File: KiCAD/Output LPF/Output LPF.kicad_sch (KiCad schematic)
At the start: 77 parts, among them J1 Conn_Coaxial_Small, J16 Screw_Terminal_01x02, J2 8P8C_Shielded, J25 Screw_Terminal_01x02, J26 Screw_Terminal_01x02, J27 Screw_Terminal_01x02, J28 Filter In, J29 Screw_Terminal_01x02, K1 Relay_RSS-SR042P, K10 Relay_RSS-SR042P, K2 Relay_RSS-SR042P, K3 Relay_RSS-SR042P, K4 Relay_RSS-SR042P, K5 Relay_RSS-SR042P, K6 Relay_RSS-SR042P, K7 Relay_RSS-SR042P, K8 Relay_RSS-SR042P, K9 Relay_RSS-SR042P, Q1 2N7000, Q10 2N7000, Q5 2N7000, Q8 2N7000, Q9 2N7000

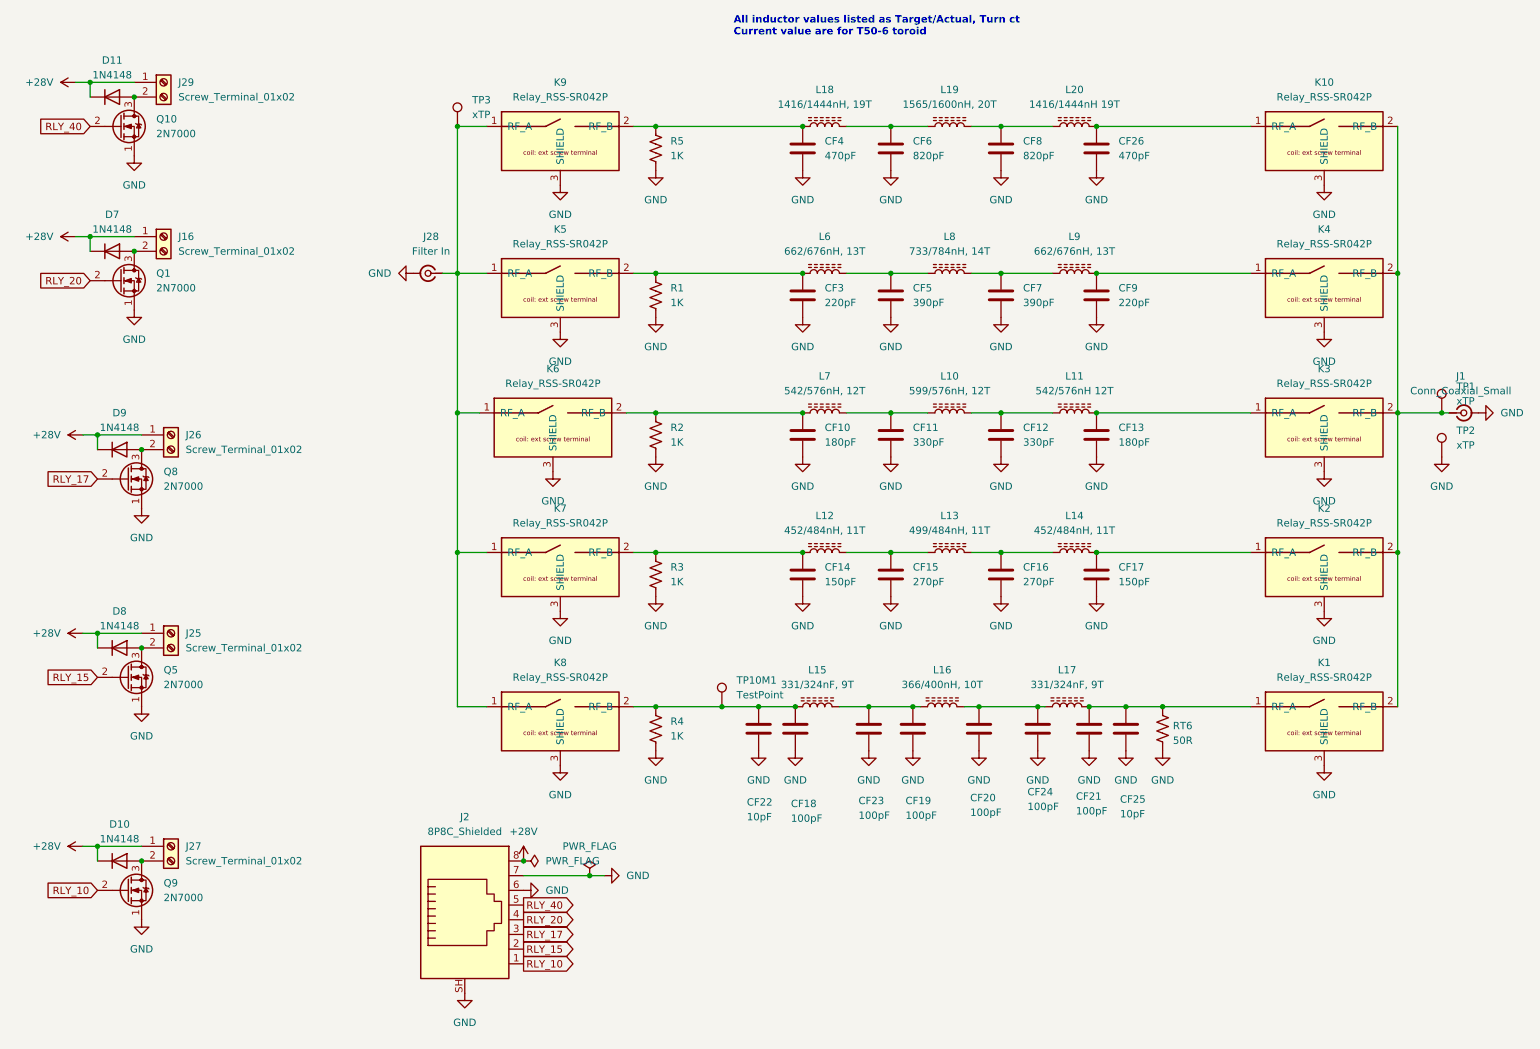
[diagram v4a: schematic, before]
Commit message: WIP revD Output LPF: 10m bank converted to G6K DPDT, library additions
Intermediate snapshot -- migration in progress.

- xmitter library: add Relay_G6K symbol (copied from stock KiCad
  Relay:G6K-2, pre-linked to xmitter:Relay_DPDT_G6K-2P-Y-T1 footprint)
  and Relay_DPDT_G6K-2P-Y-T1.kicad_mod footprint (10 x 6.5 mm body,
  -Y pitch: 3.2mm/2.2mm/2.2mm along row, 5.08mm row spacing, 0.85mm
  THT holes)
- Documentation/Components: Omron G6K-T1 datasheet
- Output LPF 10m bank: converted from K1+K8 SPST pair to single K1
  DPDT G6K. Pole 1 switches output (pin 3=COM to LPF-out, pin 4=NO
  to common J1). Pole 2 switches input (pin 6=COM to LPF-in, pin
  5=NO to common J28). K8 removed.
- Analog: WIP (details TBD when more banks converted)

Known open items before next commit:
- +12V net on LPF has no source (umbilical still carries +28V, needs
  rewire or LDO)
- 40m/20m/17m/15m banks still on old RSS-SR042P SPST topology
- Consider moving R3 to K1 pin 7 (removes 0.4 dB active-path loss,
  keeps swamp function via NC path when bank unselected)

Co-Authored-By: Claude Opus 4.7 <noreply@anthropic.com>
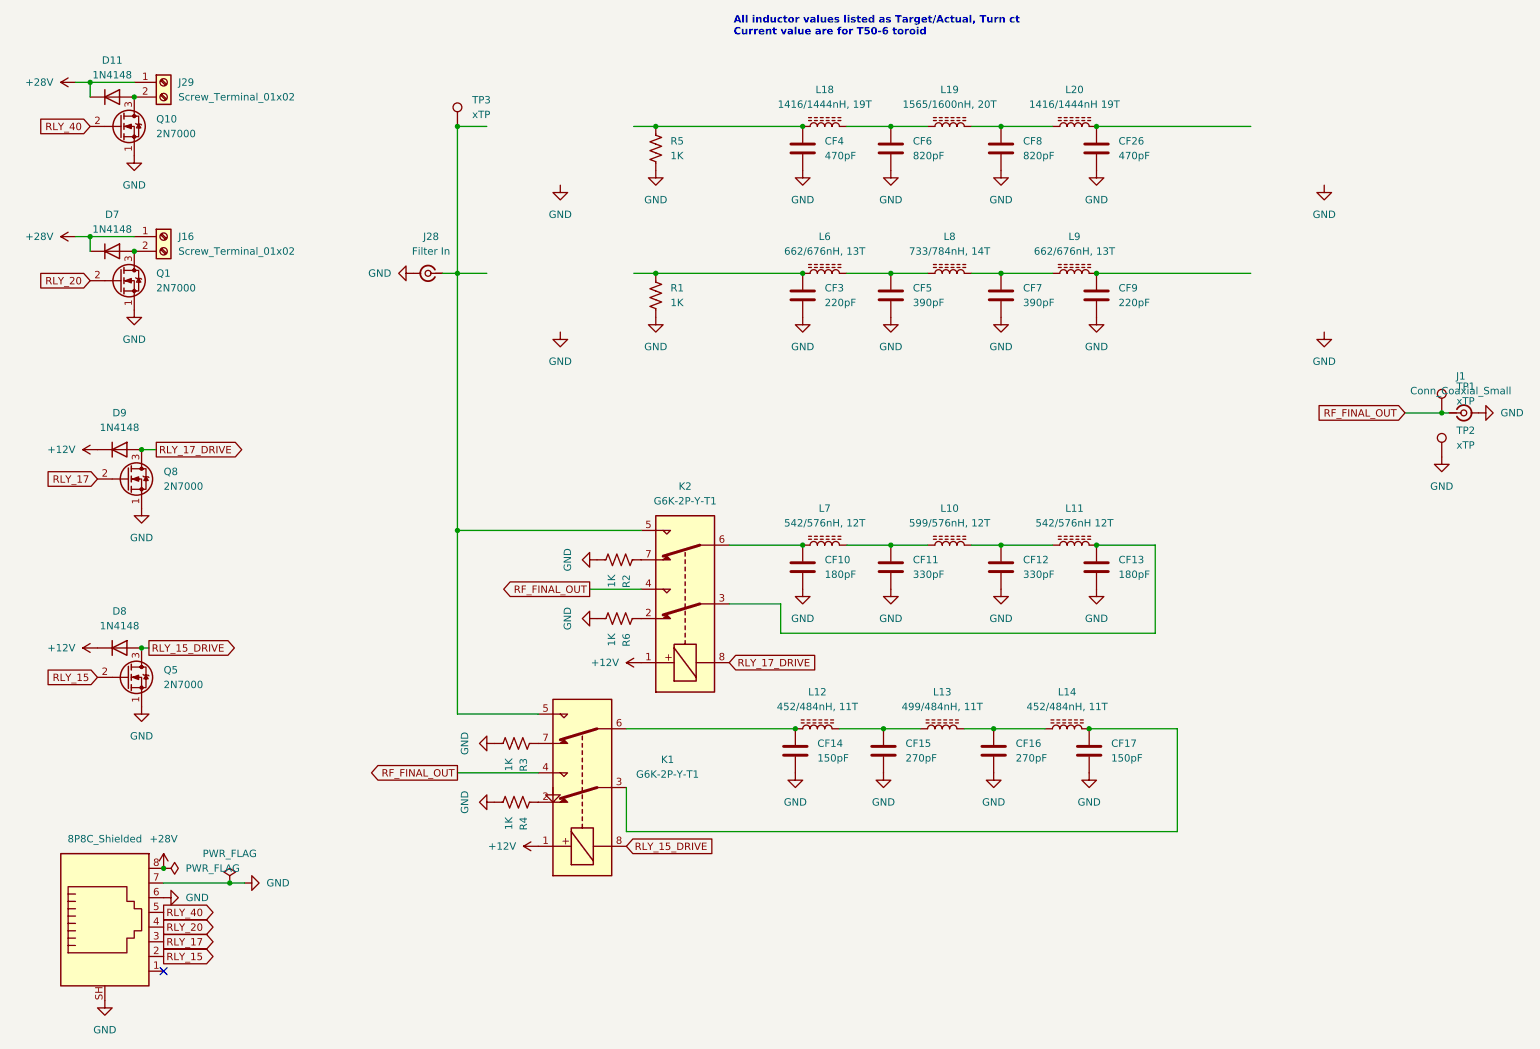
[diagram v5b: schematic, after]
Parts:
- removed CF18, CF21, CF23, CF24: 100pF, Capacitor_THT:C_Disc_D6.0mm_W2.5mm_P5.00mm, symbol Device:C
- removed CF19, CF20: 100pF, Capacitor_THT:C_Disc_D7.5mm_W2.5mm_P5.00mm, symbol Device:C
- removed CF22, CF25: 10pF, Capacitor_THT:C_Disc_D6.0mm_W2.5mm_P5.00mm, symbol Device:C
- removed D10: 1N4148, Diode_THT:D_DO-35_SOD27_P7.62mm_Horizontal, symbol Diode:1N4148
- removed J25, J26, J27: Screw_Terminal_01x02, TerminalBlock_Phoenix:TerminalBlock_Phoenix_MKDS-1,5-2_1x02_P5.00mm_Horizontal, symbol Connector:Screw_Terminal_01x02
- removed K1, K10, K2, K3, K4, K5, K6, K7, K8, K9: Relay_RSS-SR042P, xmitter:Relay_SPST_RelComm_RSS-SR042P, symbol xmitter:Relay_SPST_RSS-SR042P
- removed L15, L17: 331/324nF, 9T, xmitter:T50-6_Flat_HandWound, symbol Device:L_Ferrite
- removed L16: 366/400nH, 10T, xmitter:T50-6_Vertical_HandWound, symbol Device:L_Ferrite
- removed Q9: 2N7000, Package_TO_SOT_THT:TO-92_Inline, symbol Transistor_FET:2N7000
- removed RT6: 50R, Resistor_THT:R_Axial_DIN0207_L6.3mm_D2.5mm_P10.16mm_Horizontal, symbol Device:R_US
- removed TP10M1: TestPoint, Connector_PinHeader_2.54mm:PinHeader_1x01_P2.54mm_Vertical, symbol Connector:TestPoint
- added K1, K2: G6K-2P-Y-T1, xmitter:Relay_DPDT_G6K-2P-Y-T1, symbol xmitter:Relay_G6K
- added R6: 1K, Resistor_THT:R_Axial_DIN0207_L6.3mm_D2.5mm_P10.16mm_Horizontal, symbol Device:R_US
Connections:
- net +28V: no longer D8.1 (K), D9.1 (K)
- net GND: now also R6.2
- net RLY_17_DRIVE: now reaches D9.2 (A), Q8.3 (D)
- net RLY_17_DRIVE: now also K2.8
- net RF_FINAL_OUT: now reaches J1.1 (In), TP1.1
- net RF_FINAL_OUT: now also K1.4, K2.4
- net RLY_15_DRIVE: now reaches D8.2 (A), Q5.3 (D)
- net RLY_15_DRIVE: now also K1.8
- net at CF14.1, L12.1: now also K1.6; no longer R3.1
- net at CF17.1, L14.2: now also K1.3
- net at J28.1 (In), TP3.1: now also K1.5, K2.5
- net at CF10.1, L7.1: now also K2.6; no longer R2.1
- net at R4.1: now also K1.2
- net at CF13.1, L11.2: now also K2.3
- net RLY_10: no longer names the net of J2.1
- new net: K2.7, R2.1
- new net: K2.2, R6.1
- new net: K1.7, R3.1
- new net +12V: D8.1 (K), D9.1 (K), K1.1, K2.1
- no-connect marks 0 -> 1
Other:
- moved on the sheet: CF10, CF11, CF12, CF13, CF14, CF15, CF16, CF17, L10, L11, L12, L13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

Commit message: revD: drop 10m, convert LPF to DPDT G6K throughout, retire +28V rail
Output LPF:
- 10m bank removed (K8/K1-equivalent, L15/L16/L17, CF14-CF25 and
  parallel-cap combos, R4 original). 10m to be handled via main rig.
- All 4 remaining bands now use a single xmitter:Relay_G6K DPDT per
  bank (K1=15m, K2=17m, K3=20m, K4=40m). Pole 1 switches output,
  Pole 2 switches input. Half the relay count vs the old SPST pair.
- Coil chain per bank: pin1=+12V, pin8=RLY_xx_DRIVE via 2N7000
  (Q5/Q8/Q1/Q10 for 15/17/20/40) with 1N4148 flyback (D7/D8/D9/D11).
- Swamp resistors (R2-R9, 2 per bank) placed on relay pin 7 (NC) so
  they only load the LPF when the bank is unselected -- removes
  active-path insertion loss.
- Legacy screw terminals J16/J25/J26/J27/J29 and +28V coil feed
  deleted. Umbilical now carries +12V on J2 pin 8.

Analog:
- LT1054 +28V voltage doubler (U9) and its support caps/diodes
  removed. +28V net purged from every sheet.
- +12V (LM2940CT-12 U8) now feeds the LPF coil supply via J2 pin 8.
- LT1054 -12V inverter (U7) retained for LM7171 negative rail.
- +12V current budget: ~75-100 mA worst case (op-amp rails + one
  G6K coil active) against 1 A LDO capacity.

Co-Authored-By: Claude Opus 4.7 <noreply@anthropic.com>
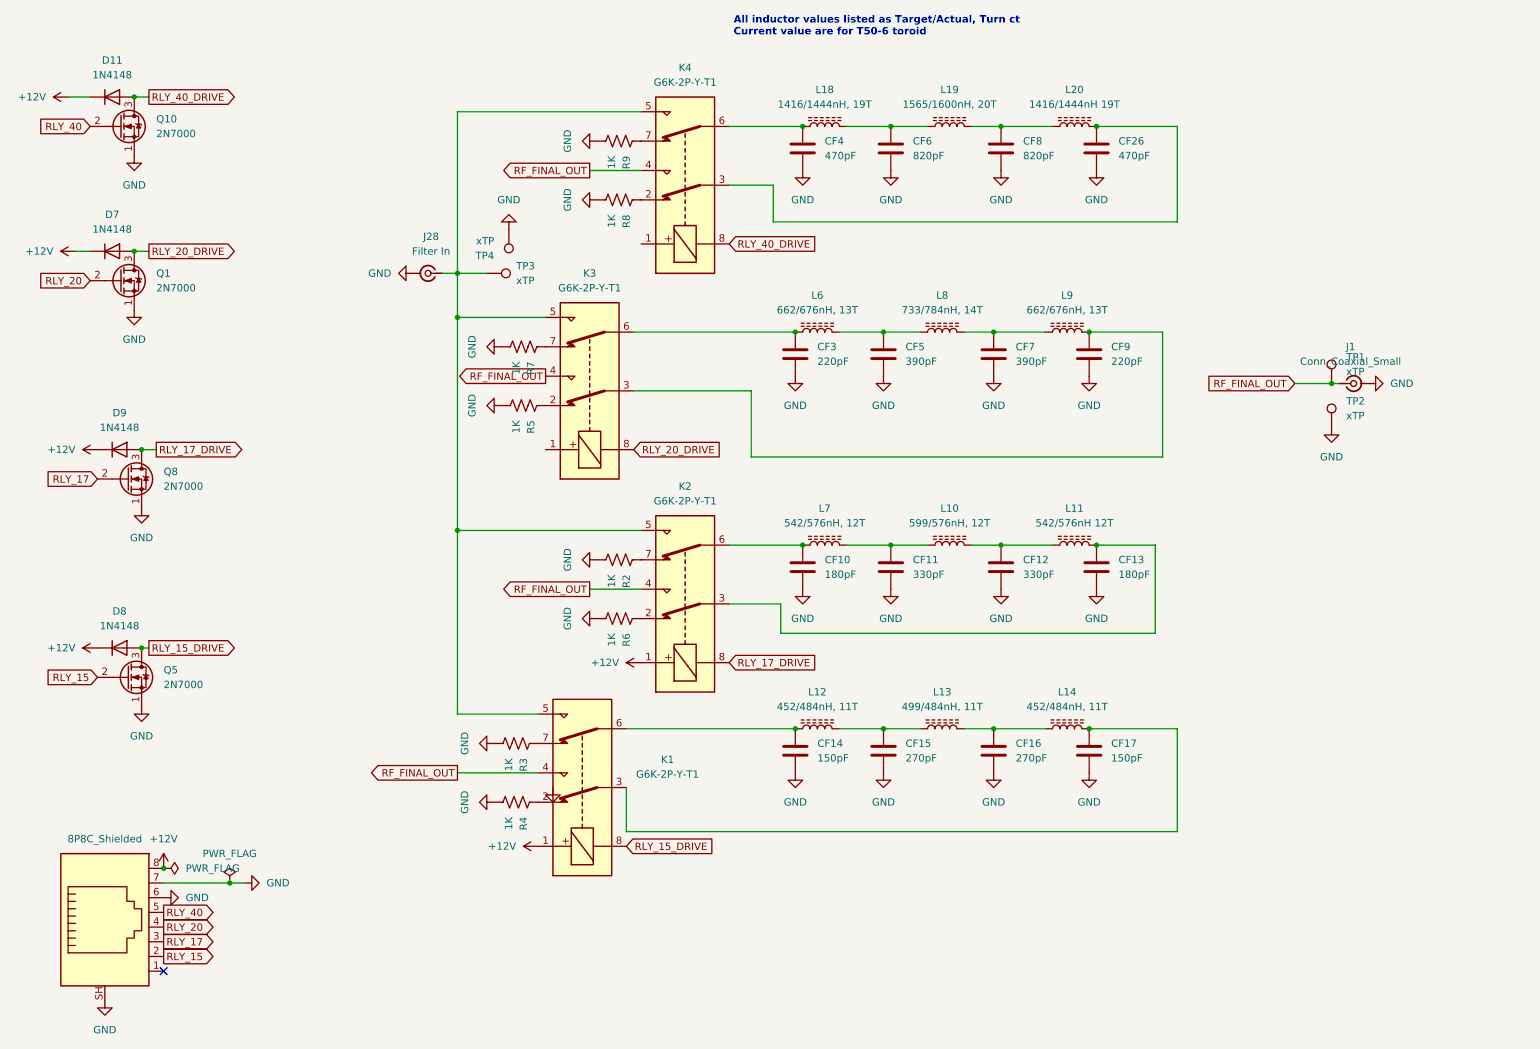
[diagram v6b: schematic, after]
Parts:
- removed J16, J29: Screw_Terminal_01x02, TerminalBlock_Phoenix:TerminalBlock_Phoenix_MKDS-1,5-2_1x02_P5.00mm_Horizontal, symbol Connector:Screw_Terminal_01x02
- removed R1: 1K, Resistor_THT:R_Axial_DIN0207_L6.3mm_D2.5mm_P10.16mm_Horizontal, symbol Device:R_US
- added K3, K4: G6K-2P-Y-T1, xmitter:Relay_DPDT_G6K-2P-Y-T1, symbol xmitter:Relay_G6K
- added R7, R8, R9: 1K, Resistor_THT:R_Axial_DIN0207_L6.3mm_D2.5mm_P10.16mm_Horizontal, symbol Device:R_US
- added TP4: xTP, Connector_PinHeader_2.54mm:PinHeader_1x01_P2.54mm_Vertical, symbol xmitter:xTP
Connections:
- net +28V is gone; now on net +12V: D11.1 (K), D7.1 (K), J2.8
- net GND: now also R7.2, R8.2, R9.2, TP4.1
- net RF_FINAL_OUT: now also K3.4, K4.4
- net at CF3.1, L6.1: now also K3.6
- net RLY_40_DRIVE: now reaches D11.2 (A), Q10.3 (D)
- net RLY_40_DRIVE: now also K4.8
- net at CF9.1, L9.2: now also K3.3
- net at J28.1 (In), K1.5, K2.5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: now also K3.5, K4.5
- net at CF4.1, L18.1: now also K4.6; no longer R5.1
- net at CF26.1, L20.2: now also K4.3
- net RLY_20_DRIVE: now reaches D7.2 (A), Q1.3 (D)
- net RLY_20_DRIVE: now also K3.8
- new net: K4.2, R8.1
- new net: K4.7, R9.1
- new net: K3.7, R7.1
- new net: K3.2, R5.1
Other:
- moved on the sheet: CF3, CF5, CF7, CF9, J1, L6, L8, L9, TP1, TP2

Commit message: revD Output LPF: swap R2-R9 to 50R + ERC fixes
- R2-R9 (per-bank swamps on K-relay pin 7) changed from 1k to 50R.
  With both ends terminated via NC path when the bank is unselected,
  50 ohm makes the unselected LPF a properly-terminated two-port --
  kills internal LC resonances and gives maximum isolation against
  active-bank leakage.
- ERC errors fixed in KiCad after the resistor-value edit.

Co-Authored-By: Claude Opus 4.7 <noreply@anthropic.com>
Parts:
- R2, R3, R4, R5, R6, R7, R8, R9: value 1K -> 50R
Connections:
- net +12V: now also K3.1, K4.1
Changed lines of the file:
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@@
 			)
 		)
-		(property "Value" "1K"
+		(property "Value" "50R"
 			(at 119.3801 111.76 0)
 			(show_name no)
@@
 			)
 		)
-		(property "Value" "1K"
+		(property "Value" "50R"
 			(at 102.8701 74.93 0)
 			(show_name no)
@@
 			)
 		)
-		(property "Value" "1K"
+		(property "Value" "50R"
 			(at 101.6001 143.51 0)
 			(show_name no)
@@
 			)
 		)
-		(property "Value" "1K"
+		(property "Value" "50R"
 			(at 119.3801 49.53 0)
 			(show_name no)
@@
 			)
 		)
-		(property "Value" "1K"
+		(property "Value" "50R"
 			(at 119.3801 121.92 0)
 			(show_name no)
@@
 			)
 		)
-		(property "Value" "1K"
+		(property "Value" "50R"
 			(at 102.8701 85.09 0)
 			(show_name no)
@@
 			)
 		)
-		(property "Value" "1K"
+		(property "Value" "50R"
 			(at 101.6001 153.67 0)
 			(show_name no)
@@
 	)
 	(symbol
-		(lib_id "power:GND")
-		(at 109.22 148.59 0)
-		(unit 1)
-		(body_style 1)
-		(exclude_from_sim no)
-		(in_bom yes)
-		(on_board yes)
-		(in_pos_files yes)
-		(dnp no)
-		(fields_autoplaced yes)
-		(property "Reference" "#PWR011"
-			(at 109.22 154.94 0)
-			(hide yes)
-			(show_name no)
-			(do_not_autoplace no)
-			(effects
-				(font
-					(size 1.27 1.27)
-				)
-			)
-		)
-		(property "Value" "GND"
-			(at 109.22 153.67 0)
-			(hide yes)
-			(show_name no)
-			(do_not_autoplace no)
-			(effects
-				(font
-					(size 1.27 1.27)
-				)
-			)
-		)
-		(property "Footprint" ""
-			(at 109.22 148.59 0)
-			(hide yes)
-			(show_name no)
-			(do_not_autoplace no)
-			(effects
-				(font
-					(size 1.27 1.27)
-				)
-			)
-		)
-		(property "Datasheet" ""
-			(at 109.22 148.59 0)
-			(hide yes)
-			(show_name no)
-			(do_not_autoplace no)
-			(effects
-				(font
-					(size 1.27 1.27)
-				)
-			)
-		)
-		(property "Description" "Power symbol creates a global label with name \"GND\" , ground"
-			(at 109.22 148.59 0)
-			(hide yes)
-			(show_name no)
-			(do_not_autoplace no)
-			(effects
-				(font
-					(size 1.27 1.27)
-				)
-			)
-		)
-		(pin "1"
-		)
-		(instances
-			(project "Output LPF"
-				(path "/007eb1af-0bdc-4199-b14f-f7b02ad55c1c"
-					(reference "#PWR011")
-					(unit 1)
-				)
-			)
-		)
-	)
-	(symbol
 		(lib_id "Device:L_Ferrite")
 		(at 154.94 69.85 90)
@@
 			)
 		)
-		(property "Value" "1K"
+		(property "Value" "50R"
 			(at 119.3801 39.37 0)
 			(show_name no)
@@
 	)
 	(symbol
+		(lib_id "power:+12V")
+		(at 107.95 90.17 90)
+		(unit 1)
+		(body_style 1)
+		(exclude_from_sim no)
+		(in_bom yes)
+		(on_board yes)
+		(in_pos_files yes)
+		(dnp no)
+		(fields_autoplaced yes)
+		(property "Reference" "#PWR023"
+			(at 111.76 90.17 0)
+			(hide yes)
+			(show_name no)
+			(do_not_autoplace no)
+			(effects
+				(font
+					(size 1.27 1.27)
+				)
+			)
+		)
+		(property "Value" "+12V"
+			(at 104.14 90.1699 90)
+			(show_name no)
+			(do_not_autoplace no)
+			(effects
+				(font
+					(size 1.27 1.27)
+				)
+				(justify left)
+			)
+		)
+		(property "Footprint" ""
+			(at 107.95 90.17 0)
+			(hide yes)
+			(show_name no)
+			(do_not_autoplace no)
+			(effects
+				(font
+					(size 1.27 1.27)
+				)
+			)
+		)
+		(property "Datasheet" ""
+			(at 107.95 90.17 0)
+			(hide yes)
+			(show_name no)
+			(do_not_autoplace no)
+			(effects
+				(font
+					(size 1.27 1.27)
+				)
+			)
+		)
+		(property "Description" "Power symbol creates a global label with name \"+12V\""
+			(at 107.95 90.17 0)
+			(hide yes)
+			(show_name no)
+			(do_not_autoplace no)
+			(effects
+				(font
+					(size 1.27 1.27)
+				)
+			)
+		)
+		(pin "1"
+		)
+		(instances
+			(project "Output LPF"
+				(path "/007eb1af-0bdc-4199-b14f-f7b02ad55c1c"
+					(reference "#PWR023")
+					(unit 1)
+				)
+			)
+		)
+	)
+	(symbol
 		(lib_id "Device:L_Ferrite")
 		(at 154.94 138.43 90)
@@
 					(unit 1)
 				)
+			)
+		)
+	)
+	(symbol
+		(lib_id "power:+12V")
+		(at 124.46 54.61 90)
+		(unit 1)
+		(body_style 1)
+		(exclude_from_sim no)
+		(in_bom yes)
+		(on_board yes)
+		(in_pos_files yes)
+		(dnp no)
+		(fields_autoplaced yes)
+		(property "Reference" "#PWR022"
+			(at 128.27 54.61 0)
+			(hide yes)
+			(show_name no)
+			(do_not_autoplace no)
+			(effects
+				(font
+					(size 1.27 1.27)
+				)
+			)
+		)
+		(property "Value" "+12V"
+			(at 120.65 54.6099 90)
+			(show_name no)
+			(do_not_autoplace no)
+			(effects
+				(font
+					(size 1.27 1.27)
+				)
+				(justify left)
+			)
+		)
+		(property "Footprint" ""
+			(at 124.46 54.61 0)
+			(hide yes)
+			(show_name no)
+			(do_not_autoplace no)
+			(effects
+				(font
+					(size 1.27 1.27)
+				)
+			)
+		)
+		(property "Datasheet" ""
+			(at 124.46 54.61 0)
+			(hide yes)
+			(show_name no)
+			(do_not_autoplace no)
+			(effects
+				(font
+					(size 1.27 1.27)
+				)
+			)
+		)
+		(property "Description" "Power symbol creates a global label with name \"+12V\""
+			(at 124.46 54.61 0)
+			(hide yes)
+			(show_name no)
+			(do_not_autoplace no)
+			(effects
+				(font
+					(size 1.27 1.27)
+				)
+			)
+		)
+		(pin "1"
+		)
+		(instances
+			(project "Output LPF"
+				(path "/007eb1af-0bdc-4199-b14f-f7b02ad55c1c"
+					(reference "#PWR022")
+					(unit 1)
+				)
